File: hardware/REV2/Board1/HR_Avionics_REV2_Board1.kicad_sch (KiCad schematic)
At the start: 150 parts, among them J1 Conn_01x02_Socket, J10 Conn_01x02_Socket, J11 Conn_01x02_Socket, J12 Conn_01x03_Socket, J2 Conn_01x02_Socket, J3 Conn_01x02_Socket, J4 Conn_01x02_Socket, J5 Conn_01x02_Socket, J6 Conn_01x02_Socket, J7 Conn_01x06_Socket, J8 Conn_01x02_Socket, J9 Conn_01x03_Socket, Q1 TJ60S04M3L(T6L,1NQ, Q10 TJ60S04M3L(T6L,1NQ, Q11 BSS138, Q12 BSS138, Q13 BSS138, Q2 TJ60S04M3L(T6L,1NQ, Q3 TJ60S04M3L(T6L,1NQ, Q4 TJ60S04M3L(T6L,1NQ, Q5 MTB7D0N06RJ3, Q6 MTB7D0N06RJ3, Q7 MTB7D0N06RJ3, Q8 MTB7D0N06RJ3, Q9 TJ60S04M3L(T6L,1NQ, U1 LTC4353, U16 USBLC6-4SC6, U18 TCAN3414DR, U2 AZ1117CH-3.3TRG1, U3 MCP1402T-E_OT, U4 STM32F303K8Tx, U5 SSM6J808RLF, U6 SSM6J808RLF, U7 INA219AIDR, U8 LMR51635, U9 MCP1402T-E_OT, Y2 CSTNE16M0V530000R0

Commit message: Update PCB
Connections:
- net at D10.1 (K), J12.2 (Pin_2), J9.2 (Pin_2)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: now also FL1.3; no longer FL1.2
- net at D10.2 (K), J12.1 (Pin_1), J9.1 (Pin_1)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: now also FL1.2; no longer FL1.3
- net at U18.6 (CANL): now also FL1.4; no longer FL1.1
- net at U18.7 (CANH): now also FL1.1; no longer FL1.4

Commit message: Update PCB
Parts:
- removed R53: 0, Resistor_SMD:R_0603_1608Metric_Pad0.98x0.95mm_HandSolder, symbol Device:R_Small
- added J15, J16, J17, J18: S2711-46R, pq_k_gentaro:S2711-46R, symbol Connector_Generic:Conn_01x01
- added U10: S01-30300500, Unknown:S01-30300500, symbol Unknown:S01-30300500
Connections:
- net GND: now also D18.2 (A2), D3.2 (A2), D5.2 (A2), D6.2 (A2), J15.1 (Pin_1), J16.1 (Pin_1), J17.1 (Pin_1), J18.1 (Pin_1); no longer D18.1 (A1), D3.1 (A1), D5.1 (A1), D6.1 (A1)
- net VDC: now also U8.2 (EN)
- net at C21.1, D4.1 (K), F1.1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: now also D18.1 (A1); no longer D18.2 (A2)
- net at D8.2 (A), J4.2 (Pin_2), Q8.2 (D): now also D6.1 (A1); no longer D6.2 (A2)
- net at D4.2 (A), J3.2 (Pin_2), Q7.2 (D): now also D5.1 (A1); no longer D5.2 (A2)
- net at C26.1, D8.1 (K), F2.1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: now also D3.1 (A1); no longer D3.2 (A2)
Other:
- note added: "S2711-46R"
- moved on the sheet: D18, D3, D5, D6

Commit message: Update PCB
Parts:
- F3, F5, F6: footprint Capacitor_SMD:C_1210_3225Metric_Pad1.33x2.70mm_HandSolder -> Fuse:Fuse_1210_3225Metric_Pad1.42x2.65mm_HandSolder

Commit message: Add system diagram in shcematic
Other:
- note added: "5V(合計3Aまで)"
- note added: "Board1"
- note removed: "5V"
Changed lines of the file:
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@@
 (kicad_sch
-	(version 20250114)
+	(version 20260306)
 	(generator "eeschema")
-	(generator_version "9.0")
+	(generator_version "10.0")
 	(paper "A1")
 	(title_block

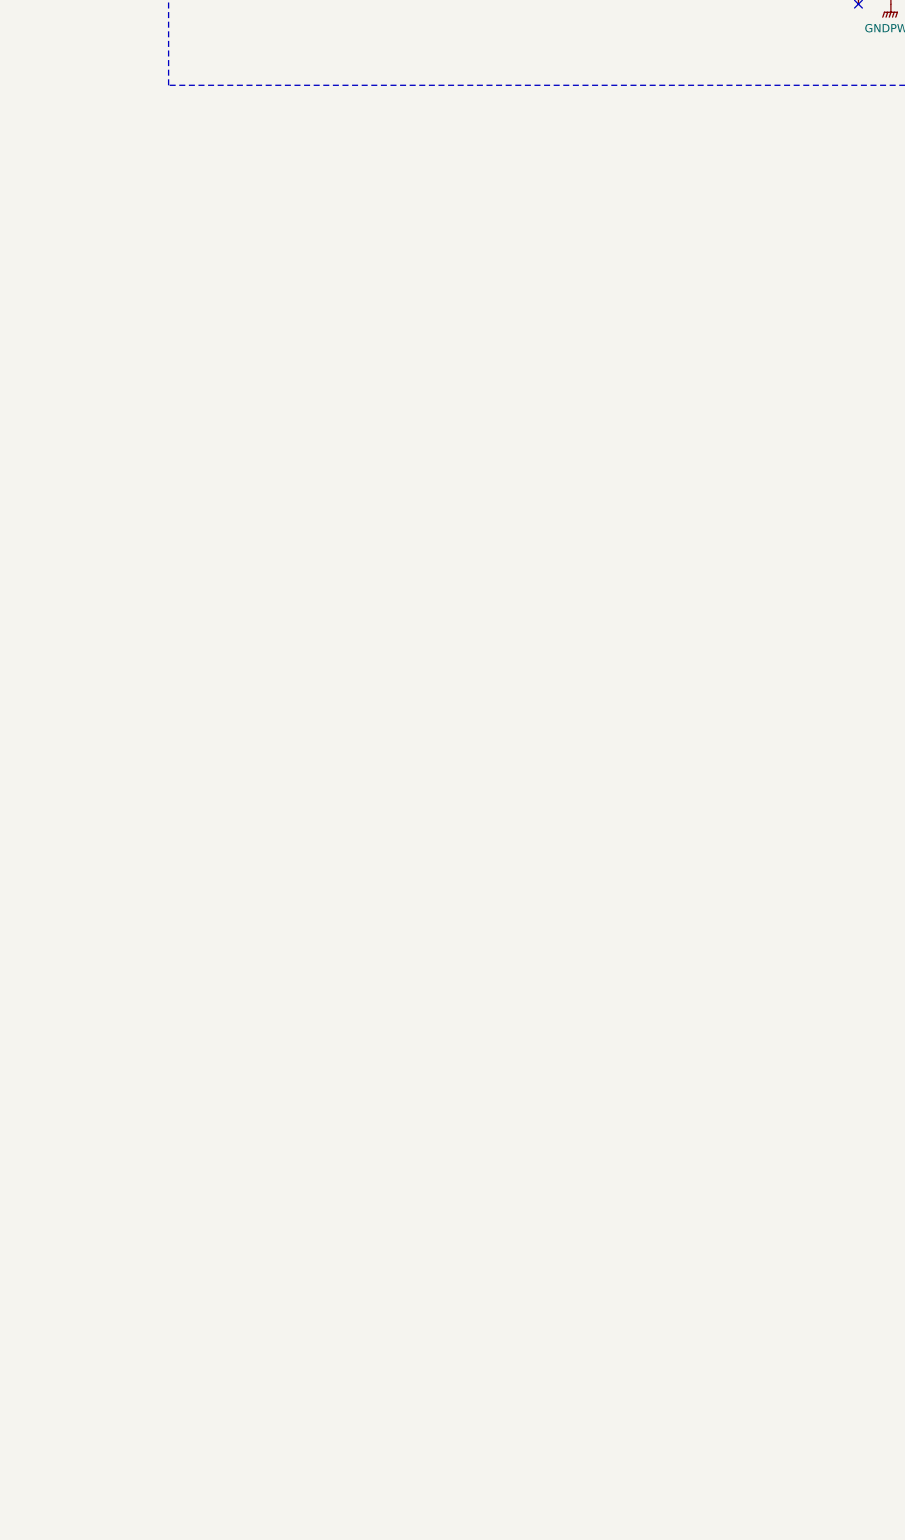
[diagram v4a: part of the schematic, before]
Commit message: Add Power Supply and System diagram
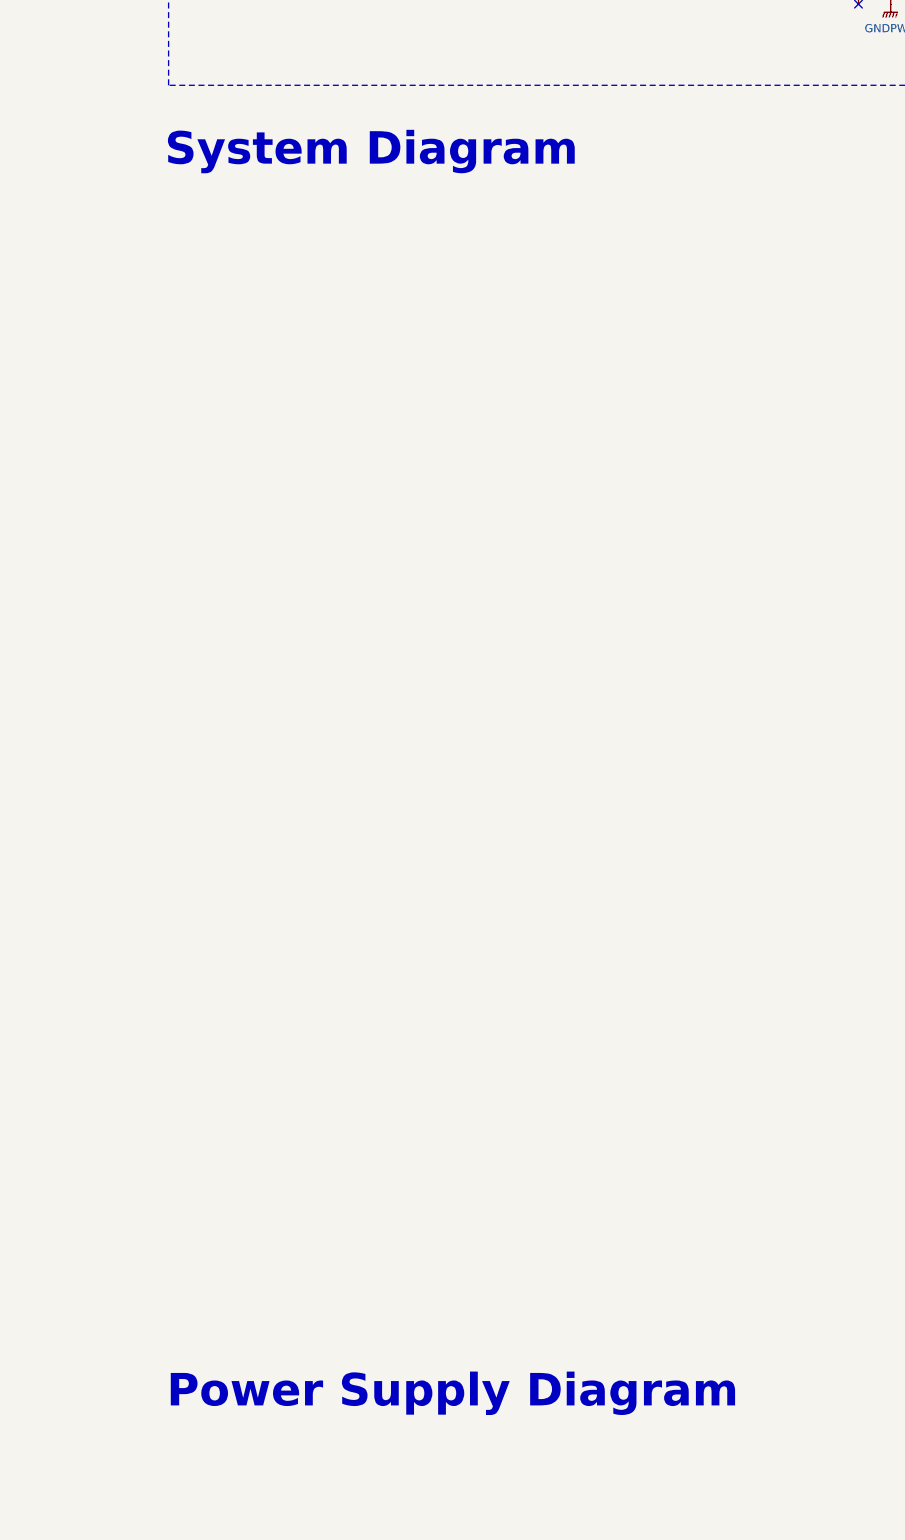
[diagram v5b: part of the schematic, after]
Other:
- note added: "Power Supply Diagram"
- note added: "System Diagram"
